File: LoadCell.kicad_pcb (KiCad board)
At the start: 2 copper layers, 50.8 x 25.4 mm, 18 parts, among them J1 Vin, J2 GND, J3 WHT, J4 GRN, J5 RED, J6 BLK, J7 Vout, J8 GND, U1 L78L12ABUTR, U2 LM321SN3T1G

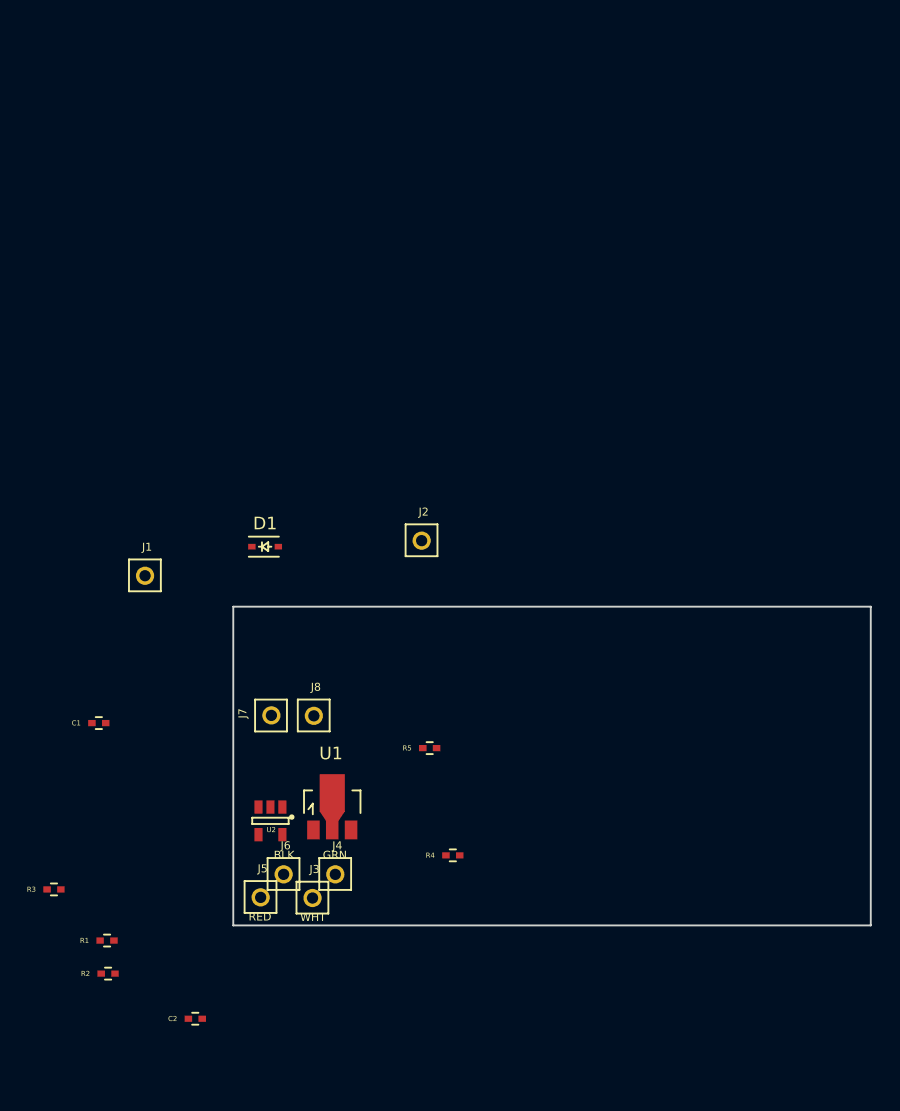
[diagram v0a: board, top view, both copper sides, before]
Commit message: Single circuit placed
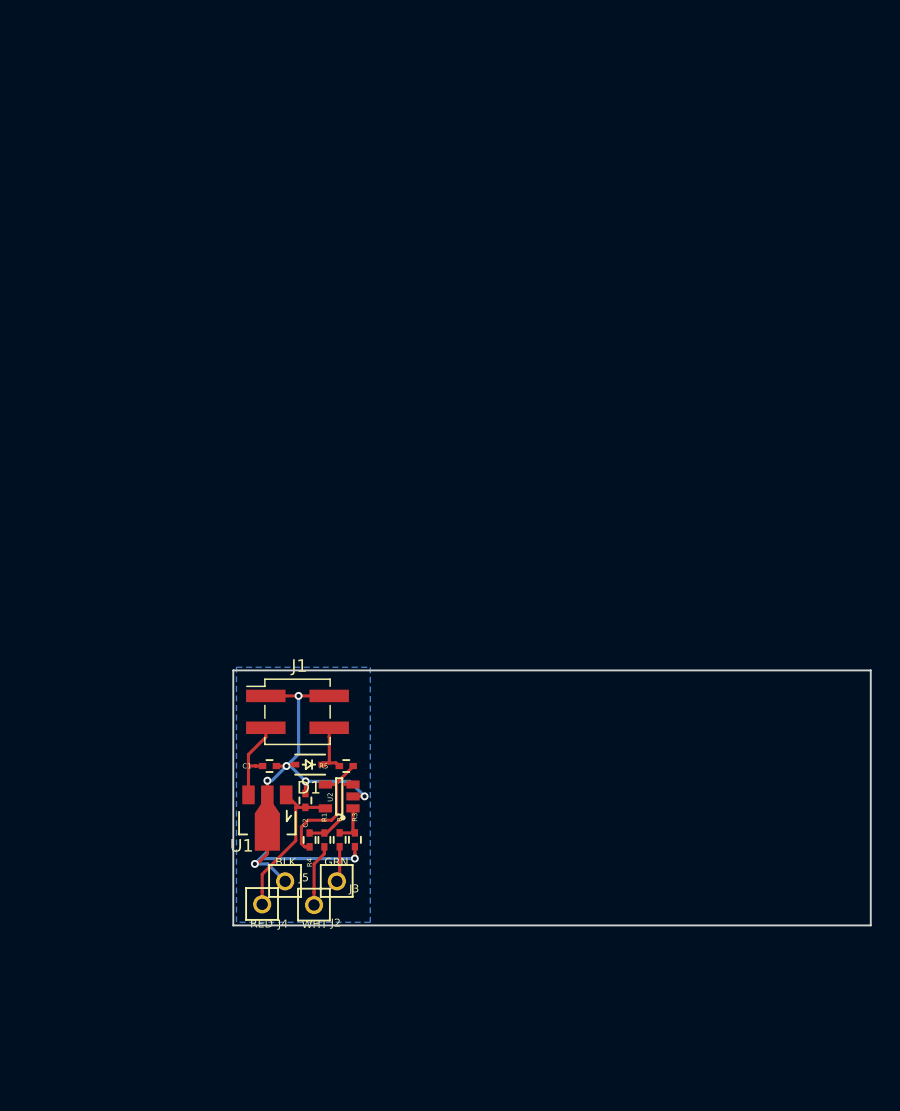
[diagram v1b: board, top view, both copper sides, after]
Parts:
- removed the J2 at (116.6, 70.9)
- removed J7: Vout, _Connector:0.100_1x1_small
- removed J8: GND, _Connector:0.100_1x1_small
- J1: value Vin -> CONN_02X02; footprint _Connector:0.100_1x1_small -> _Connector:Pin_Header_Straight_2x02_Pitch2.54mm_SMD
- moved R3 24.3 mm to (111.3, 94.8), turned to 270 degrees
- moved R2 21.3 mm to (110.1, 94.8), turned to 270 degrees
- moved C2 19.5 mm to (107.3, 91.6), turned to 90 degrees
- moved R1 19.1 mm to (108.9, 94.8), turned to 270 degrees
- moved D1 17.7 mm to (107.6, 88.8), turned to 180 degrees
- moved J1 16.3 mm to (106.7, 84.6)
- moved C1 14.0 mm to (104.5, 88.9)
- moved R4 11.5 mm to (107.7, 94.8), turned to 90 degrees
- moved R5 6.80 mm to (110.6, 88.9)
- moved U2 5.81 mm to (110.0, 91.3), turned to 180 degrees
- moved U1 5.25 mm to (104.3, 93.1), turned to 180 degrees
- moved J2 0.57 mm to (108.0, 100.0)
- moved J3 0.57 mm to (109.9, 98.1)
- moved J5 0.57 mm to (105.7, 98.1)
- moved J4 0.57 mm to (103.9, 99.9)
- renumbered J3 to J2, J4 to J3, J5 to J4, J6 to J5
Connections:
- C1 pad 1: Net-(C1-Pad1) -> /Main Sheet/Vin
- D1 pad 1: Net-(D1-Pad1) -> /Main Sheet/Vout
- J1 pad 1: Net-(C1-Pad1) -> GND
- R5 pad 1: Net-(D1-Pad1) -> /Main Sheet/Vout
- U1 pad 3: Net-(C1-Pad1) -> /Main Sheet/Vin
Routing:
- net GND: track 0.00 -> 51.1 mm, vias 0 -> 7
- net +12V: track 0.00 -> 12.6 mm
- net Net-(R4-Pad1): track 0.00 -> 10.7 mm
- net /Main Sheet/Vin: track 0.00 -> 7.05 mm
- net Net-(R1-Pad1): track 0.00 -> 6.53 mm
- net Net-(J2-Pad1): track 0.00 -> 4.97 mm
- net /Main Sheet/Vout: track 0.00 -> 4.26 mm
- net Net-(R2-Pad1): track 0.00 -> 3.24 mm
- net Net-(J3-Pad1): track 0.00 -> 2.85 mm
- added copper zone on B.Cu, net GND
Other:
- board size 50.8 x 25.4 mm -> 50.8 x 20.3 mm
- rule trace_min: 0.2 -> 0.20066
- rule via_min_drill: 0.3 -> 0.3302
- rule via_min_size: 0.4 -> 0.3302

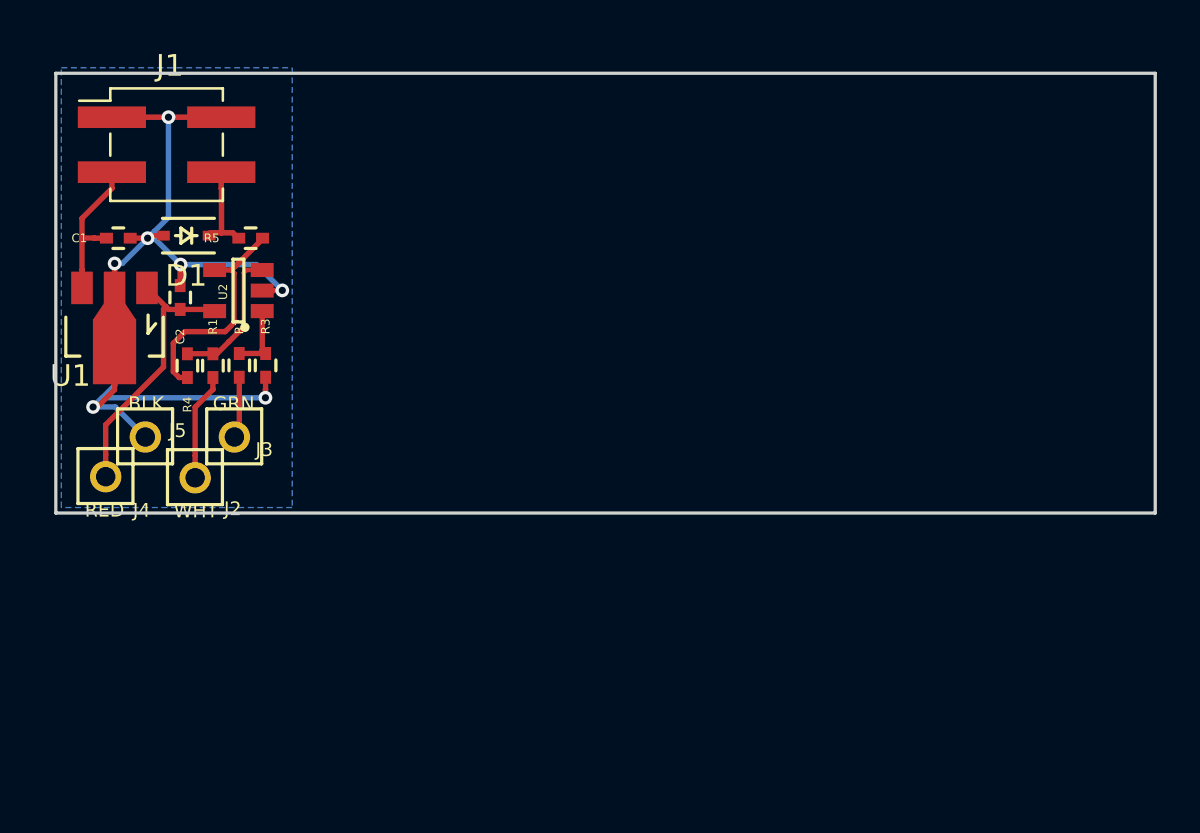
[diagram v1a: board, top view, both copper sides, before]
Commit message: Revised circuit. Schematic revised, layout not yet.
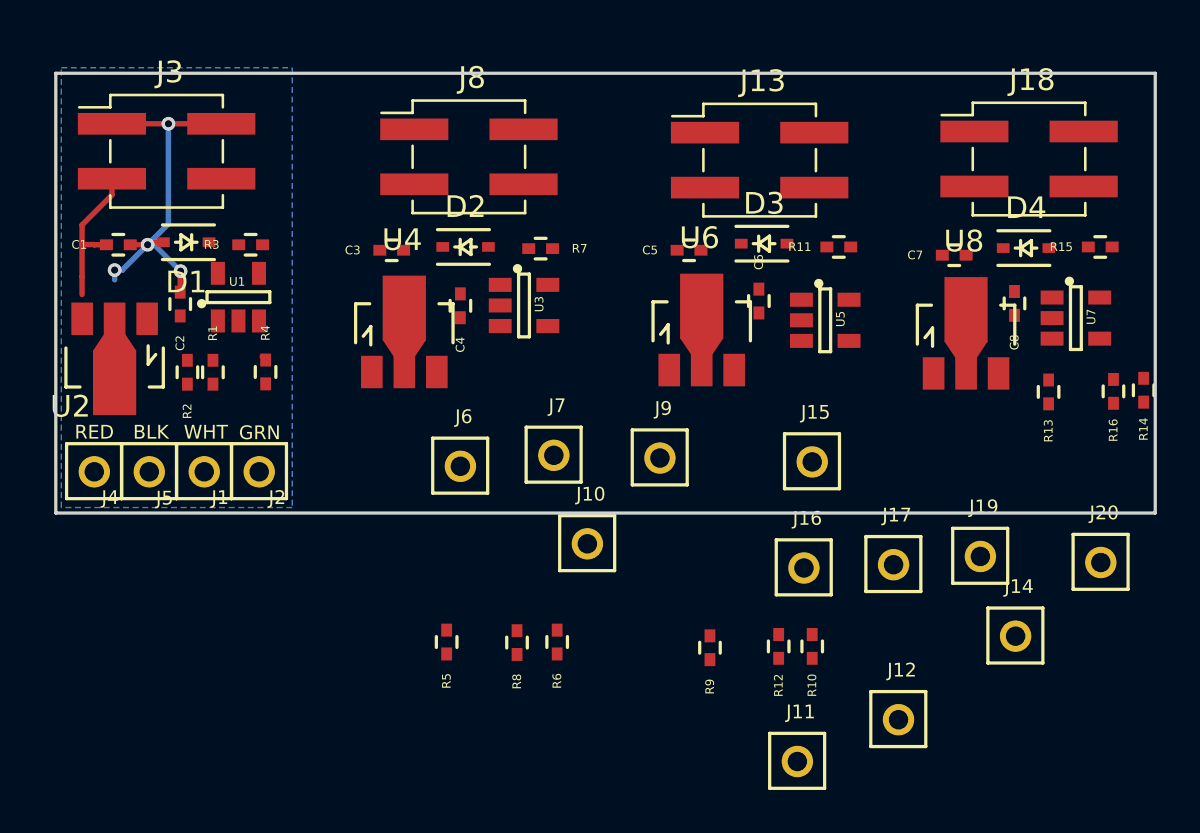
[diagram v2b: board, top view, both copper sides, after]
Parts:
- removed the R2 at (110.1, 94.8)
- added C3: 1uF, _Passive:C_0402, F.Cu at (117.1, 89.5)
- added C4: 1uF, _Passive:C_0402, F.Cu at (120.3, 92.0)
- added C5: 1uF, _Passive:C_0402, F.Cu at (130.9, 89.5)
- added C6: 1uF, _Passive:C_0402, F.Cu at (134.1, 91.8)
- added C7: 1uF, _Passive:C_0402, F.Cu at (143.1, 89.7)
- added C8: 1uF, _Passive:C_0402, F.Cu at (145.9, 91.9)
- added D2: MM3Z3V0ST1G, _Passive:SOD-323, F.Cu at (120.5, 89.3)
- added D3: MM3Z3V0ST1G, _Passive:SOD-323, F.Cu at (134.3, 89.2)
- added D4: MM3Z3V0ST1G, _Passive:SOD-323, F.Cu at (146.4, 89.4)
- added J10: BLK, _Connector:0.100_1x1_small, F.Cu at (126.2, 103.0)
- added J11: WHT, _Connector:0.100_1x1_small, F.Cu at (135.9, 113.1)
- added J12: GRN, _Connector:0.100_1x1_small, F.Cu at (140.5, 111.2)
- added J13: M20-8760242, _Connector:Pin_Header_Straight_2x02_Pitch2.54mm_SMD, F.Cu at (134.1, 85.3)
- added J14: RED, _Connector:0.100_1x1_small, F.Cu at (145.9, 107.3)
- added J15: BLK, _Connector:0.100_1x1_small, F.Cu at (136.6, 99.2)
- added J16: WHT, _Connector:0.100_1x1_small, F.Cu at (136.2, 104.1)
- added J17: GRN, _Connector:0.100_1x1_small, F.Cu at (140.3, 104.0)
- added J18: M20-8760242, _Connector:Pin_Header_Straight_2x02_Pitch2.54mm_SMD, F.Cu at (146.6, 85.2)
- added J19: RED, _Connector:0.100_1x1_small, F.Cu at (144.3, 103.6)
- added J20: BLK, _Connector:0.100_1x1_small, F.Cu at (149.9, 103.9)
- added J6: WHT, _Connector:0.100_1x1_small, F.Cu at (120.3, 99.4)
- added J7: GRN, _Connector:0.100_1x1_small, F.Cu at (124.6, 98.9)
- added J8: M20-8760242, _Connector:Pin_Header_Straight_2x02_Pitch2.54mm_SMD, F.Cu at (120.7, 85.1)
- added J9: RED, _Connector:0.100_1x1_small, F.Cu at (129.5, 99.1)
- added R10: 270K, _Passive:R_0402, F.Cu at (136.6, 107.8)
- added R11: 100R, _Passive:R_0402, F.Cu at (137.8, 89.3)
- added R12: 100R, _Passive:R_0402, F.Cu at (135.0, 107.8)
- added R13: 1K, _Passive:R_0402, F.Cu at (147.5, 96.0)
- added R14: 270K, _Passive:R_0402, F.Cu at (151.9, 95.9)
- added R15: 100R, _Passive:R_0402, F.Cu at (149.9, 89.3)
- added R16: 100R, _Passive:R_0402, F.Cu at (150.5, 96.0)
- added R5: 1K, _Passive:R_0402, F.Cu at (119.7, 107.6)
- added R6: 270K, _Passive:R_0402, F.Cu at (124.8, 107.6)
- added R7: 100R, _Passive:R_0402, F.Cu at (124.0, 89.4)
- added R8: 100R, _Passive:R_0402, F.Cu at (122.9, 107.6)
- added R9: 1K, _Passive:R_0402, F.Cu at (131.8, 107.8)
- added U3: LM321SN3T1G, _Active:SOT-23-5, F.Cu at (123.2, 92.0)
- added U4: L78L12ABUTR, _Active:SOT89-3, F.Cu at (117.7, 93.2)
- added U5: LM321SN3T1G, _Active:SOT-23-5, F.Cu at (137.2, 92.7)
- added U6: L78L12ABUTR, _Active:SOT89-3, F.Cu at (131.4, 93.1)
- added U7: LM321SN3T1G, _Active:SOT-23-5, F.Cu at (148.7, 92.6)
- added U8: L78L12ABUTR, _Active:SOT89-3, F.Cu at (143.7, 93.3)
- D1: value D_ZENER -> MM3Z3V0ST1G
- J3: renamed from J1; value CONN_02X02 -> M20-8760242
- R1: value 100R -> 1K
- R2: renamed from R4; value 10K -> 270K
- R4: renamed from R3; value 10K -> 100R
- moved J2 1.97 mm to (111.0, 99.7)
- moved J5 1.62 mm to (105.9, 99.7)
- moved U2 1.42 mm to (104.3, 94.5)
- moved J4 0.57 mm to (103.4, 99.7)
- moved J1 0.50 mm to (108.5, 99.7)
- moved C1 0.30 mm to (104.5, 89.2)
- moved C2 0.30 mm to (107.3, 91.9)
- moved D1 0.30 mm to (107.6, 89.1)
- moved J3 0.30 mm to (106.7, 84.9)
- moved R1 0.30 mm to (108.9, 95.1)
- moved R2 0.30 mm to (107.7, 95.1)
- moved R3 0.30 mm to (110.6, 89.2)
- moved R4 0.30 mm to (111.3, 95.1)
- moved U1 0.30 mm to (110.0, 91.6), turned to 90 degrees
- renumbered J2 to J1, J3 to J2, R5 to R3, U2 to U1, U1 to U2
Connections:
- net +12V renamed Net-(C2-Pad1)
- net Net-(R1-Pad1) renamed /Main Sheet/Vin-
- net Net-(R4-Pad1) renamed /Main Sheet/Vo
- J2 pad 1: Net-(J3-Pad1) -> /Main Sheet/Vin+
- R4 pad 1: Net-(R2-Pad1) -> /Main Sheet/Vout
- U1 pad 1: Net-(R2-Pad1) -> /Main Sheet/Vin+
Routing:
- net GND: track 51.1 -> 18.1 mm, vias 7 -> 4
- net Net-(C2-Pad1): track 12.6 -> 0.00 mm
- net /Main Sheet/Vo: track 10.7 -> 0.00 mm
- net /Main Sheet/Vin-: track 6.53 -> 0.00 mm
- net Net-(J1-Pad1): track 4.97 -> 0.00 mm
- net /Main Sheet/Vout: track 4.26 -> 0.22 mm
- net Net-(R2-Pad1): track 3.24 -> 0.00 mm
- net Net-(J3-Pad1): track 2.85 -> 0.00 mm

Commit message: First unit layout
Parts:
- removed the J1 at (108.5, 99.7)
- removed J10, J15, J20: BLK, _Connector:0.100_1x1_small
- removed J11, J16: WHT, _Connector:0.100_1x1_small
- removed J12, J17: GRN, _Connector:0.100_1x1_small
- removed J13, J18: M20-8760242, _Connector:Pin_Header_Straight_2x02_Pitch2.54mm_SMD
- removed J14, J19, J9: RED, _Connector:0.100_1x1_small
- added J3: M20-8760242, _Connector:Pin_Header_Straight_2x02_Pitch2.54mm_SMD, F.Cu at (120.5, 86.4)
- J2: value GRN -> 0.100_1X4; footprint _Connector:0.100_1x1_small -> _Connector:0.100_1x4_small
- J4: value RED -> 0.100_1X4; footprint _Connector:0.100_1x1_small -> _Connector:0.100_1x4_small
- J5: value BLK -> M20-8760242; footprint _Connector:0.100_1x1_small -> _Connector:Pin_Header_Straight_2x02_Pitch2.54mm_SMD
- J6: value WHT -> 0.100_1X4; footprint _Connector:0.100_1x1_small -> _Connector:0.100_1x4_small
- J7: value GRN -> M20-8760242; footprint _Connector:0.100_1x1_small -> _Connector:Pin_Header_Straight_2x02_Pitch2.54mm_SMD
- J8: value M20-8760242 -> 0.100_1X4; footprint _Connector:Pin_Header_Straight_2x02_Pitch2.54mm_SMD -> _Connector:0.100_1x4_small
- R10, R14, R6: value 270K -> 1K
- R13, R5, R9: value 1K -> 270K
- U3, U5, U7: value LM321SN3T1G -> L78L12ABUTR; footprint _Active:SOT-23-5 -> _Active:SOT89-3
- U4, U6, U8: value L78L12ABUTR -> LM321SN3T1G; footprint _Active:SOT89-3 -> _Active:SOT-23-5
- moved J5 30.8 mm to (133.7, 86.4)
- moved J8 30.0 mm to (146.8, 99.8), turned to 90 degrees
- moved J7 25.6 mm to (146.9, 86.4)
- moved R12 17.8 mm to (136.8, 90.1), turned to 180 degrees
- moved R8 17.5 mm to (123.8, 90.1), turned to 180 degrees
- moved J4 17.0 mm to (120.4, 99.8), turned to 90 degrees
- moved J6 13.3 mm to (133.6, 99.8), turned to 90 degrees
- moved R9 12.0 mm to (137.8, 97.4), turned to 0 degrees
- moved R5 11.4 mm to (124.8, 97.4), turned to 0 degrees
- moved R6 10.5 mm to (122.3, 97.4), turned to 0 degrees
- moved R10 10.5 mm to (135.2, 97.4), turned to 0 degrees
- moved U5 6.75 mm to (130.8, 95.0)
- moved U8 6.50 mm to (150.0, 94.6), turned to 90 degrees
- moved U3 6.37 mm to (117.6, 95.0)
- moved U4 6.07 mm to (123.6, 94.6), turned to 90 degrees
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- renumbered J3 to J1, R2 to R1, R1 to R2, U2 to U1, U1 to U2
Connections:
- net /Main Sheet/Vin- renamed /Main Sheet/VL-
- net /Main Sheet/Vo renamed /Main Sheet/Vopo
- C2 pad 1: Net-(C2-Pad1) -> /Main Sheet/RED
- C4 pad 1: /Main Sheet/Vcc -> Net-(C4-Pad1)
- J2 pad 1: /Main Sheet/Vin+ -> /Main Sheet/RED
- J4 pad 1: Net-(C2-Pad1) -> Net-(C4-Pad1)
- J6 pad 1: Net-(J6-Pad1) -> Net-(C6-Pad1)
- J7 pad 1: Net-(J7-Pad1) -> GND
- J8 pad 1: GND -> Net-(C8-Pad1)
- J8 pad 3: Net-(C3-Pad1) -> Net-(J8-Pad3)
- J8 pad 4: Net-(D2-Pad1) -> Net-(J8-Pad4)
- R10 pad 2: Net-(R10-Pad2) -> Net-(J6-Pad4)
- R11 pad 2: Net-(R10-Pad1) -> Net-(R11-Pad2)
- R13 pad 2: Net-(J16-Pad1) -> Net-(R13-Pad2)
- R14 pad 1: Net-(R14-Pad1) -> Net-(R13-Pad2)
- R14 pad 2: Net-(R13-Pad1) -> Net-(J8-Pad4)
- R15 pad 2: Net-(R14-Pad1) -> Net-(R13-Pad1)
- R2 pad 2: Net-(J1-Pad1) -> /Main Sheet/WHT
- R5 pad 2: Net-(J6-Pad1) -> Net-(R5-Pad2)
- R6 pad 1: Net-(R6-Pad1) -> Net-(R5-Pad2)
- R6 pad 2: Net-(R5-Pad1) -> Net-(J4-Pad4)
- R7 pad 2: Net-(R6-Pad1) -> Net-(R5-Pad1)
- R9 pad 1: Net-(R10-Pad2) -> Net-(R11-Pad2)
- R9 pad 2: Net-(J11-Pad1) -> Net-(R10-Pad1)
- U1 pad 1: Net-(C2-Pad1) -> /Main Sheet/RED
- U2 pad 1: /Main Sheet/Vin+ -> /Main Sheet/GRN
- U2 pad 5: Net-(C2-Pad1) -> /Main Sheet/RED
- U3 pad 1: Net-(J7-Pad1) -> Net-(C4-Pad1)
- U3 pad 3: Net-(R5-Pad1) -> Net-(C3-Pad1)
- U4 pad 1: /Main Sheet/Vcc -> Net-(J4-Pad3)
- U4 pad 3: Net-(C3-Pad1) -> Net-(R5-Pad2)
- U5 pad 1: Net-(J12-Pad1) -> Net-(C6-Pad1)
- U5 pad 3: Net-(R10-Pad2) -> Net-(C5-Pad1)
- U6 pad 1: Net-(C6-Pad1) -> Net-(J6-Pad3)
- U6 pad 3: Net-(C5-Pad1) -> Net-(R10-Pad1)
- U7 pad 1: Net-(J17-Pad1) -> Net-(C8-Pad1)
- U7 pad 3: Net-(R13-Pad1) -> Net-(C7-Pad1)
- U8 pad 1: Net-(C8-Pad1) -> Net-(J8-Pad3)
- U8 pad 3: Net-(C7-Pad1) -> Net-(R13-Pad2)
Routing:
- net GND: track 18.1 -> 42.4 mm, vias 4 -> 7
- net /Main Sheet/RED: track 0.00 -> 13.0 mm
- net /Main Sheet/Vout: track 0.22 -> 8.46 mm
- net /Main Sheet/Vopo: track 0.00 -> 7.17 mm
- net /Main Sheet/GRN: track 0.00 -> 5.25 mm
- net /Main Sheet/WHT: track 0.00 -> 3.63 mm
- net /Main Sheet/VL-: track 0.00 -> 3.34 mm
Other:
- board size 50.8 x 20.3 mm -> 50.8 x 18.5 mm
- board text added: "RED BLK GRN WHT"
